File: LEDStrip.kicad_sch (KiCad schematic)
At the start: 14 parts, among them Q1 BC517, Q2 BC516, U1 LM555xN

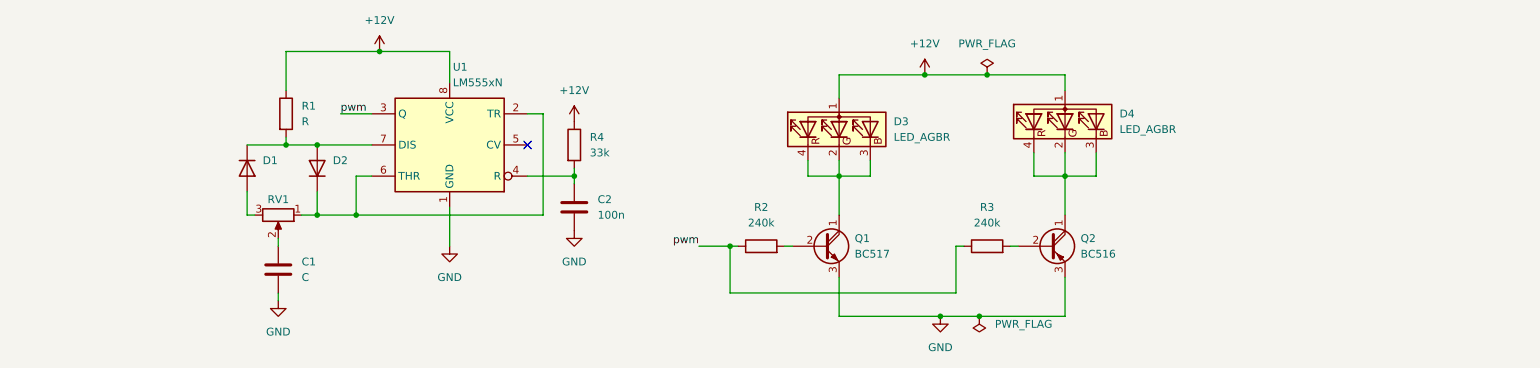
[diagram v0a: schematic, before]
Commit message: -Added group brightness control
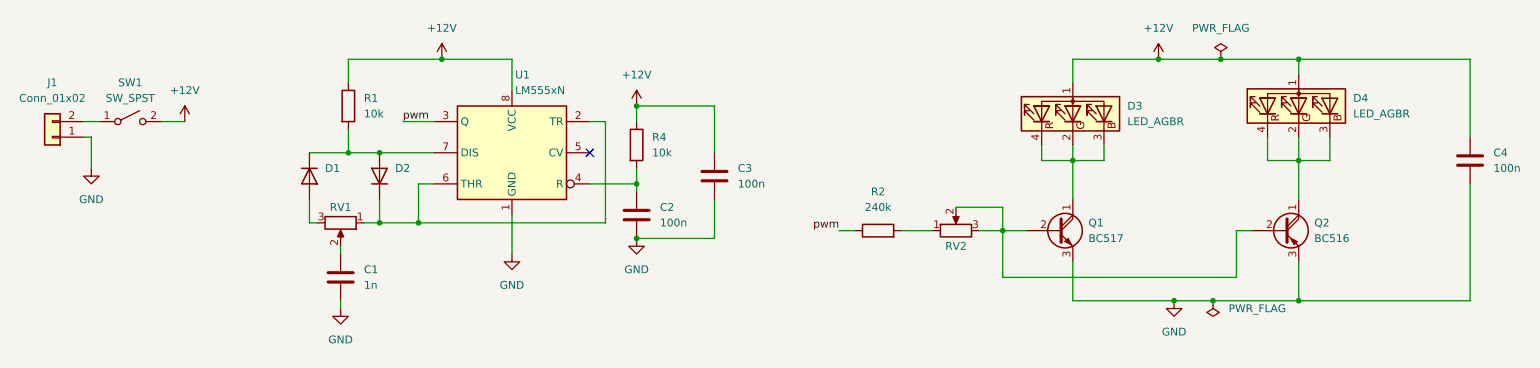
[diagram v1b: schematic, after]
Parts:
- removed R3: 240k, symbol Device:R
- added C3, C4: 100n, Capacitor_THT:C_Disc_D5.0mm_W2.5mm_P5.00mm, symbol Device:C
- added J1: Conn_01x02, Connector_PinHeader_2.54mm:PinHeader_1x02_P2.54mm_Vertical, symbol Connector_Generic:Conn_01x02
- added RV2: 220k, Potentiometer_THT:Potentiometer_ACP_CA9-V10_Vertical_Hole, symbol Device:R_Potentiometer
- added SW1: SW_SPST, Connector_PinHeader_2.54mm:PinHeader_1x03_P2.54mm_Vertical, symbol Switch:SW_SPST
- C1: value C -> 1n; footprint (none) -> Capacitor_THT:C_Disc_D5.0mm_W2.5mm_P5.00mm
- C2: footprint (none) -> Capacitor_THT:C_Disc_D5.0mm_W2.5mm_P5.00mm
- D1, D2: footprint (none) -> Diode_THT:D_A-405_P7.62mm_Horizontal
- D3, D4: footprint (none) -> Connector_PinHeader_2.54mm:PinHeader_1x02_P2.54mm_Vertical
- R1: value R -> 10k; footprint (none) -> Resistor_THT:R_Axial_DIN0207_L6.3mm_D2.5mm_P7.62mm_Horizontal
- R2: footprint (none) -> Resistor_THT:R_Axial_DIN0207_L6.3mm_D2.5mm_P7.62mm_Horizontal
- R4: value 33k -> 10k; footprint (none) -> Resistor_THT:R_Axial_DIN0207_L6.3mm_D2.5mm_P7.62mm_Horizontal
- RV1: value R_Potentiometer -> 10k; footprint (none) -> Potentiometer_THT:Potentiometer_ACP_CA9-V10_Vertical_Hole
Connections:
- net +12V: now also C3.1, C4.1, SW1.2 (B)
- net GND: now also C3.2, C4.2, J1.1 (Pin_1)
- net at Q2.2 (B): now also Q1.2 (B), RV2.2, RV2.3
- net at R2.2: now also RV2.1; no longer Q1.2 (B)
- new net: J1.2 (Pin_2), SW1.1 (A)
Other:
- moved on the sheet: C1, C2, D1, D2, D3, D4, Q1, Q2, R1, R4, RV1, U1
